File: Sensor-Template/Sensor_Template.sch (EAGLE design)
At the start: 2 parts, among them J1 TWIG-2.0-DIP

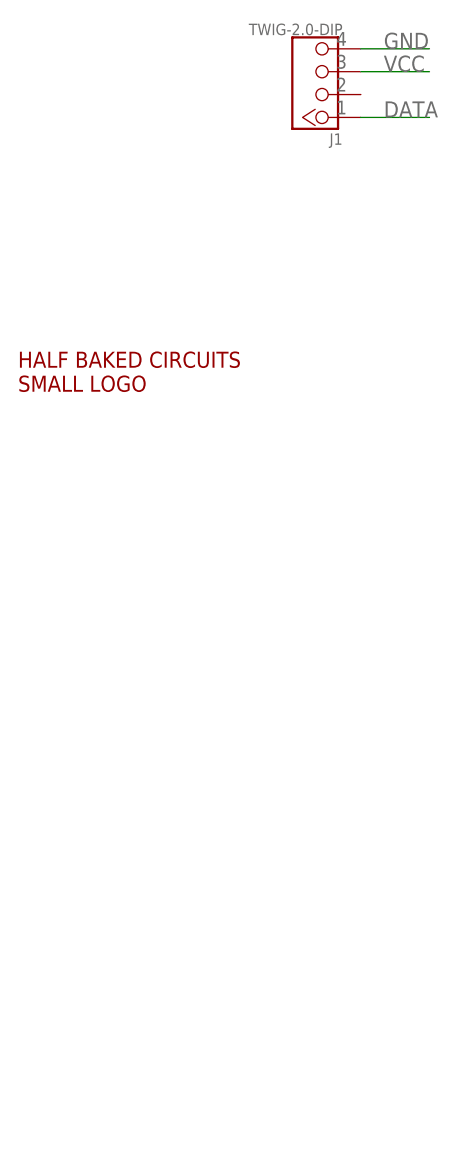
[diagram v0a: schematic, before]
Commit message: Revised Sensor Template
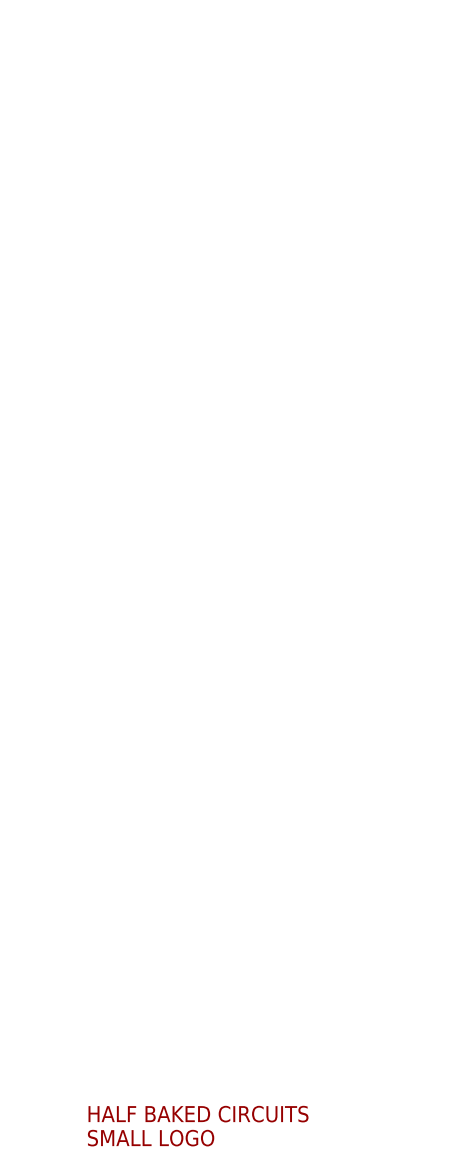
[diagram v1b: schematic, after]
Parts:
- removed J1: TWIG-2.0-DIP, Connector:TWIG-2.0-DIP
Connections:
- removed net DATA: J1.1
- removed net GND: J1.4
- removed net VCC: J1.3
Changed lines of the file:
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@@
 <layer number="54" name="bGND_GNDA" color="1" fill="9" visible="no" active="no"/>
 <layer number="56" name="wert" color="7" fill="1" visible="no" active="no"/>
+<layer number="57" name="tCAD" color="7" fill="1" visible="no" active="no"/>
+<layer number="59" name="tCarbon" color="7" fill="1" visible="no" active="no"/>
+<layer number="60" name="bCarbon" color="7" fill="1" visible="no" active="no"/>
 <layer number="90" name="Modules" color="5" fill="1" visible="yes" active="yes"/>
 <layer number="91" name="Nets" color="2" fill="1" visible="yes" active="yes"/>
@@
 <layer number="97" name="Info" color="7" fill="1" visible="yes" active="yes"/>
 <layer number="98" name="Guide" color="6" fill="1" visible="yes" active="yes"/>
+<layer number="99" name="SpiceOrder" color="7" fill="1" visible="yes" active="yes"/>
 <layer number="100" name="Muster" color="7" fill="1" visible="no" active="no"/>
 <layer number="101" name="DISIGN_HISTORY" color="3" fill="1" visible="no" active="yes"/>
@@
 <layer number="106" name="bPlate" color="7" fill="1" visible="yes" active="yes"/>
 <layer number="107" name="Crop" color="7" fill="1" visible="yes" active="yes"/>
+<layer number="108" name="centerline" color="7" fill="1" visible="yes" active="yes"/>
+<layer number="109" name="ref-old" color="7" fill="1" visible="yes" active="yes"/>
+<layer number="110" name="fp0" color="7" fill="1" visible="yes" active="yes"/>
+<layer number="111" name="LPC17xx" color="7" fill="1" visible="yes" active="yes"/>
+<layer number="112" name="tSilk" color="7" fill="1" visible="yes" active="yes"/>
+<layer number="113" name="IDFDebug" color="7" fill="1" visible="yes" active="yes"/>
+<layer number="114" name="Badge_Outline" color="7" fill="1" visible="yes" active="yes"/>
+<layer number="115" name="ReferenceISLANDS" color="7" fill="1" visible="yes" active="yes"/>
 <layer number="116" name="Patch_BOT" color="9" fill="4" visible="no" active="yes"/>
+<layer number="118" name="Rect_Pads" color="7" fill="1" visible="yes" active="yes"/>
 <layer number="121" name="_tsilk" color="7" fill="1" visible="no" active="yes"/>
 <layer number="122" name="_bsilk" color="7" fill="1" visible="no" active="yes"/>
+<layer number="123" name="tTestmark" color="7" fill="1" visible="yes" active="yes"/>
+<layer number="124" name="bTestmark" color="7" fill="1" visible="yes" active="yes"/>
+<layer number="125" name="_tNames" color="7" fill="1" visible="yes" active="yes"/>
+<layer number="126" name="_bNames" color="7" fill="1" visible="yes" active="yes"/>
+<layer number="127" name="_tValues" color="7" fill="1" visible="yes" active="yes"/>
+<layer number="128" name="_bValues" color="7" fill="1" visible="yes" active="yes"/>
+<layer number="129" name="Mask" color="7" fill="1" visible="yes" active="yes"/>
+<layer number="131" name="prix" color="7" fill="1" visible="yes" active="yes"/>
+<layer number="132" name="test" color="7" fill="1" visible="yes" active="yes"/>
 <layer number="144" name="DrillLegend" color="7" fill="1" visible="no" active="yes"/>
+<layer number="150" name="Notes" color="7" fill="1" visible="yes" active="yes"/>
 <layer number="151" name="HeatSink" color="14" fill="1" visible="no" active="no"/>
+<layer number="152" name="_bDocu" color="7" fill="1" visible="yes" active="yes"/>
+<layer number="153" name="FabDoc1" color="7" fill="1" visible="yes" active="yes"/>
+<layer number="154" name="FabDoc2" color="7" fill="1" visible="yes" active="yes"/>
+<layer number="155" name="FabDoc3" color="7" fill="1" visible="yes" active="yes"/>
+<layer number="156" name="tAssmbl" color="7" fill="1" visible="yes" active="yes"/>
+<layer number="157" name="bAssmbl" color="7" fill="1" visible="yes" active="yes"/>
+<layer number="199" name="Contour" color="7" fill="1" visible="yes" active="yes"/>
 <layer number="200" name="200bmp" color="1" fill="10" visible="no" active="no"/>
 <layer number="201" name="201bmp" color="2" fill="1" visible="no" active="no"/>
@@
 <layer number="215" name="215bmp" color="7" fill="1" visible="yes" active="yes"/>
 <layer number="216" name="216bmp" color="7" fill="1" visible="yes" active="yes"/>
+<layer number="217" name="217bmp" color="7" fill="1" visible="yes" active="yes"/>
+<layer number="218" name="218bmp" color="7" fill="1" visible="yes" active="yes"/>
+<layer number="219" name="219bmp" color="7" fill="1" visible="yes" active="yes"/>
+<layer number="220" name="220bmp" color="11" fill="1" visible="yes" active="yes"/>
+<layer number="221" name="221bmp" color="7" fill="1" visible="yes" active="yes"/>
+<layer number="222" name="222bmp" color="7" fill="1" visible="yes" active="yes"/>
+<layer number="223" name="223bmp" color="7" fill="1" visible="yes" active="yes"/>
+<layer number="224" name="224bmp" color="7" fill="1" visible="yes" active="yes"/>
+<layer number="225" name="225bmp" color="7" fill="1" visible="yes" active="yes"/>
+<layer number="226" name="226bmp" color="7" fill="1" visible="yes" active="yes"/>
+<layer number="227" name="227bmp" color="7" fill="1" visible="yes" active="yes"/>
+<layer number="228" name="228bmp" color="7" fill="1" visible="yes" active="yes"/>
+<layer number="229" name="229bmp" color="7" fill="1" visible="yes" active="yes"/>
+<layer number="230" name="230bmp" color="7" fill="1" visible="yes" active="yes"/>
+<layer number="231" name="Eagle3D_PG1" color="7" fill="1" visible="yes" active="yes"/>
+<layer number="232" name="Eagle3D_PG2" color="7" fill="1" visible="yes" active="yes"/>
+<layer number="233" name="Eagle3D_PG3" color="7" fill="1" visible="yes" active="yes"/>
+<layer number="248" name="Housing" color="7" fill="1" visible="yes" active="yes"/>
+<layer number="249" name="Edge" color="7" fill="1" visible="yes" active="yes"/>
 <layer number="250" name="Descript" color="3" fill="1" visible="no" active="no"/>
 <layer number="251" name="SMDround" color="12" fill="11" visible="no" active="no"/>
 <layer number="254" name="OrgLBR" color="13" fill="1" visible="no" active="no"/>
+<layer number="255" name="logo" color="7" fill="1" visible="yes" active="yes"/>
 </layers>
 <schematic xreflabel="%F%N/%S.%C%R" xrefpart="/%S.%C%R">
@@
 </classes>
 <parts>
-<part name="J1" library="Connector" deviceset="TWIG-2.0-DIP" device=""/>
 <part name="U$1" library="HalfBakedCircuits" deviceset="HBC-LOGO-SMALL" device=""/>
+<part name="FRAME1" library="frames" library_urn="urn:adsk.eagle:library:229" deviceset="DINA4_L" device=""/>
 </parts>
 <sheets>
@@
 </plain>
 <instances>
-<instance part="J1" gate="G$1" x="69.85" y="64.77" rot="R180"/>
-<instance part="U$1" gate="G$1" x="48.26" y="33.02"/>
+<instance part="U$1" gate="G$1" x="55.88" y="-50.8"/>
+<instance part="FRAME1" gate="G$1" x="-121.92" y="-81.28"/>
+<instance part="FRAME1" gate="G$2" x="40.64" y="-81.28"/>
 </instances>
 <busses>
 </busses>
 <nets>
-<net name="DATA" class="0">
-<segment>
-<wire x1="73.66" y1="60.96" x2="81.28" y2="60.96" width="0.1524" layer="91"/>
-<label x="76.2" y="60.96" size="1.778" layer="95"/>
-<pinref part="J1" gate="G$1" pin="1"/>
-</segment>
-</net>
-<net name="VCC" class="0">
-<segment>
-<wire x1="73.66" y1="66.04" x2="81.28" y2="66.04" width="0.1524" layer="91"/>
-<label x="76.2" y="66.04" size="1.778" layer="95"/>
-<pinref part="J1" gate="G$1" pin="3"/>
-</segment>
-</net>
-<net name="GND" class="0">
-<segment>
-<wire x1="73.66" y1="68.58" x2="81.28" y2="68.58" width="0.1524" layer="91"/>
-<label x="76.2" y="68.58" size="1.778" layer="95"/>
-<pinref part="J1" gate="G$1" pin="4"/>
-</segment>
-</net>
 </nets>
 </sheet>
@@
 which will not be processed correctly with this version.
 </note>
+<note version="8.2" severity="warning">
+Since Version 8.2, Eagle supports online libraries. The ids
+of those online libraries will not be understood (or retained)
+with this version.
+</note>
 </compatibility>
